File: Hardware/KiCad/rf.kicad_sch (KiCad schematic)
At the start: 38 parts, among them J8 Conn_Coaxial, U4 CC1200, Y3 40 MHz

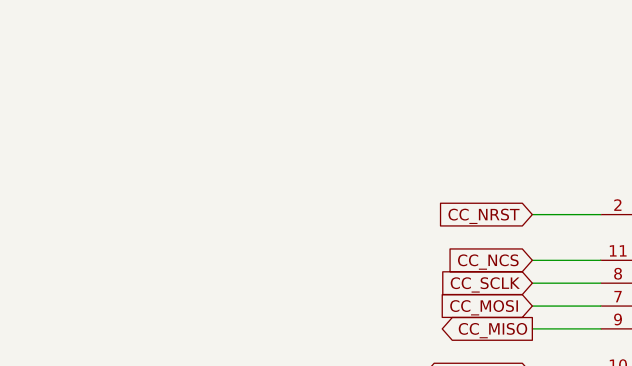
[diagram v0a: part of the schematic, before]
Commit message: Minor corrections
- fixed microphone connection and part values
- added a few TPs
- changed C27 footprint
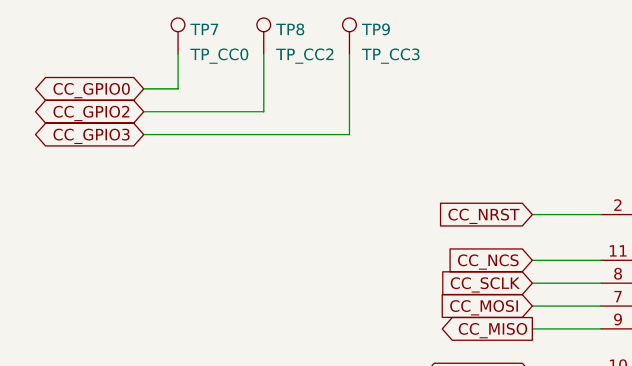
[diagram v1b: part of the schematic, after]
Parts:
- added TP7: TP_CC0, TestPoint:TestPoint_Pad_D1.0mm, symbol Connector:TestPoint
- added TP8: TP_CC2, TestPoint:TestPoint_Pad_D1.0mm, symbol Connector:TestPoint
- added TP9: TP_CC3, TestPoint:TestPoint_Pad_D1.0mm, symbol Connector:TestPoint
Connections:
- net CC_GPIO0: now also TP7.1
- net CC_GPIO2: now also TP8.1
- net CC_GPIO3: now also TP9.1
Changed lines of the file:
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@@
+    (stroke (width 0) (type default) (color 0 0 0 0))
+  )
+  (wire (pts (xy 40.64 38.1) (xy 53.975 38.1))
     (stroke (width 0) (type default) (color 0 0 0 0))
   )
@@
     (stroke (width 0) (type default) (color 0 0 0 0))
   )
+  (wire (pts (xy 53.975 38.1) (xy 53.975 31.75))
+    (stroke (width 0) (type default) (color 0 0 0 0))
+  )
   (wire (pts (xy 99.06 171.45) (xy 107.95 171.45))
     (stroke (width 0) (type default) (color 0 0 0 0))
@@
     (stroke (width 0) (type default) (color 0 0 0 0))
   )
+  (wire (pts (xy 63.5 40.64) (xy 63.5 31.75))
+    (stroke (width 0) (type default) (color 0 0 0 0))
+  )
   (wire (pts (xy 91.44 100.33) (xy 80.01 100.33))
     (stroke (width 0) (type default) (color 0 0 0 0))
@@
     (stroke (width 0) (type solid) (color 0 0 0 0))
   )
+  (wire (pts (xy 40.64 40.64) (xy 63.5 40.64))
+    (stroke (width 0) (type default) (color 0 0 0 0))
+  )
   (wire (pts (xy 52.07 92.71) (xy 54.61 92.71))
     (stroke (width 0) (type solid) (color 0 0 0 0))
@@
     (stroke (width 0) (type solid) (color 0 0 0 0))
   )
+  (wire (pts (xy 44.45 31.75) (xy 44.45 35.56))
+    (stroke (width 0) (type default) (color 0 0 0 0))
+  )
   (wire (pts (xy 54.61 92.71) (xy 54.61 95.25))
     (stroke (width 0) (type solid) (color 0 0 0 0))
+  )
+  (wire (pts (xy 40.64 35.56) (xy 44.45 35.56))
+    (stroke (width 0) (type default) (color 0 0 0 0))
   )
   (wire (pts (xy 124.46 171.45) (xy 124.46 168.91))
@@
     )
   )
+  (global_label "CC_GPIO3" (shape bidirectional) (at 40.64 40.64 180) (fields_autoplaced)
+    (effects (font (size 1.27 1.27)) (justify right))
+    (property "Intersheet References" "${INTERSHEET_REFS}" (id 0) (at 29.0345 40.5606 0)
+      (effects (font (size 1.27 1.27)) (justify right) hide)
+    )
+  )
   (global_label "LNA_N" (shape input) (at 80.01 147.32 90) (fields_autoplaced)
     (effects (font (size 1.27 1.27)) (justify left))
@@
     )
   )
+  (global_label "CC_GPIO2" (shape bidirectional) (at 40.64 38.1 180) (fields_autoplaced)
+    (effects (font (size 1.27 1.27)) (justify right))
+    (property "Intersheet References" "${INTERSHEET_REFS}" (id 0) (at 29.0345 38.0206 0)
+      (effects (font (size 1.27 1.27)) (justify right) hide)
+    )
+  )
   (global_label "CC_GPIO0" (shape bidirectional) (at 83.82 67.31 180) (fields_autoplaced)
     (effects (font (size 1.27 1.27)) (justify right))
@@
     (property "Intersheet References" "${INTERSHEET_REFS}" (id 0) (at 136.8517 100.2506 0)
       (effects (font (size 1.27 1.27)) (justify left) hide)
+    )
+  )
+  (global_label "CC_GPIO0" (shape bidirectional) (at 40.64 35.56 180) (fields_autoplaced)
+    (effects (font (size 1.27 1.27)) (justify right))
+    (property "Intersheet References" "${INTERSHEET_REFS}" (id 0) (at 29.0345 35.4806 0)
+      (effects (font (size 1.27 1.27)) (justify right) hide)
     )
   )
@@
     (pin "1")
   )
+  (symbol (lib_id "Connector:TestPoint") (at 63.5 31.75 0) (unit 1)
+    (in_bom yes) (on_board yes) (fields_autoplaced)
+    (property "Reference" "TP9" (id 0) (at 64.8971 29 0)
+      (effects (font (size 1.27 1.27)) (justify left))
+    )
+    (property "Value" "TP_CC3" (id 1) (at 64.8971 31.7751 0)
+      (effects (font (size 1.27 1.27)) (justify left))
+    )
+    (property "Footprint" "TestPoint:TestPoint_Pad_D1.0mm" (id 2) (at 68.58 31.75 0)
+      (effects (font (size 1.27 1.27)) hide)
+    )
+    (property "Datasheet" "~" (id 3) (at 68.58 31.75 0)
+      (effects (font (size 1.27 1.27)) hide)
+    )
+    (pin "1")
+  )
   (symbol (lib_id "Device:L_Small") (at 112.014 140.97 90) (unit 1)
     (in_bom yes) (on_board yes) (fields_autoplaced)
@@
     (pin "2")
   )
+  (symbol (lib_id "Connector:TestPoint") (at 53.975 31.75 0) (unit 1)
+    (in_bom yes) (on_board yes) (fields_autoplaced)
+    (property "Reference" "TP8" (id 0) (at 55.3721 29 0)
+      (effects (font (size 1.27 1.27)) (justify left))
+    )
+    (property "Value" "TP_CC2" (id 1) (at 55.3721 31.7751 0)
+      (effects (font (size 1.27 1.27)) (justify left))
+    )
+    (property "Footprint" "TestPoint:TestPoint_Pad_D1.0mm" (id 2) (at 59.055 31.75 0)
+      (effects (font (size 1.27 1.27)) hide)
+    )
+    (property "Datasheet" "~" (id 3) (at 59.055 31.75 0)
+      (effects (font (size 1.27 1.27)) hide)
+    )
+    (pin "1")
+  )
   (symbol (lib_id "power:GND") (at 165.1 91.44 0) (unit 1)
     (in_bom yes) (on_board yes)
@@
     (pin "2")
   )
+  (symbol (lib_id "Connector:TestPoint") (at 44.45 31.75 0) (unit 1)
+    (in_bom yes) (on_board yes) (fields_autoplaced)
+    (property "Reference" "TP7" (id 0) (at 45.8471 29 0)
+      (effects (font (size 1.27 1.27)) (justify left))
+    )
+    (property "Value" "TP_CC0" (id 1) (at 45.8471 31.7751 0)
+      (effects (font (size 1.27 1.27)) (justify left))
+    )
+    (property "Footprint" "TestPoint:TestPoint_Pad_D1.0mm" (id 2) (at 49.53 31.75 0)
+      (effects (font (size 1.27 1.27)) hide)
+    )
+    (property "Datasheet" "~" (id 3) (at 49.53 31.75 0)
+      (effects (font (size 1.27 1.27)) hide)
+    )
+    (pin "1")
+  )
   (symbol (lib_id "pkl_device:pkl_C_Small") (at 162.306 56.896 0) (unit 1)
